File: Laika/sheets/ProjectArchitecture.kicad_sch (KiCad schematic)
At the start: 0 parts

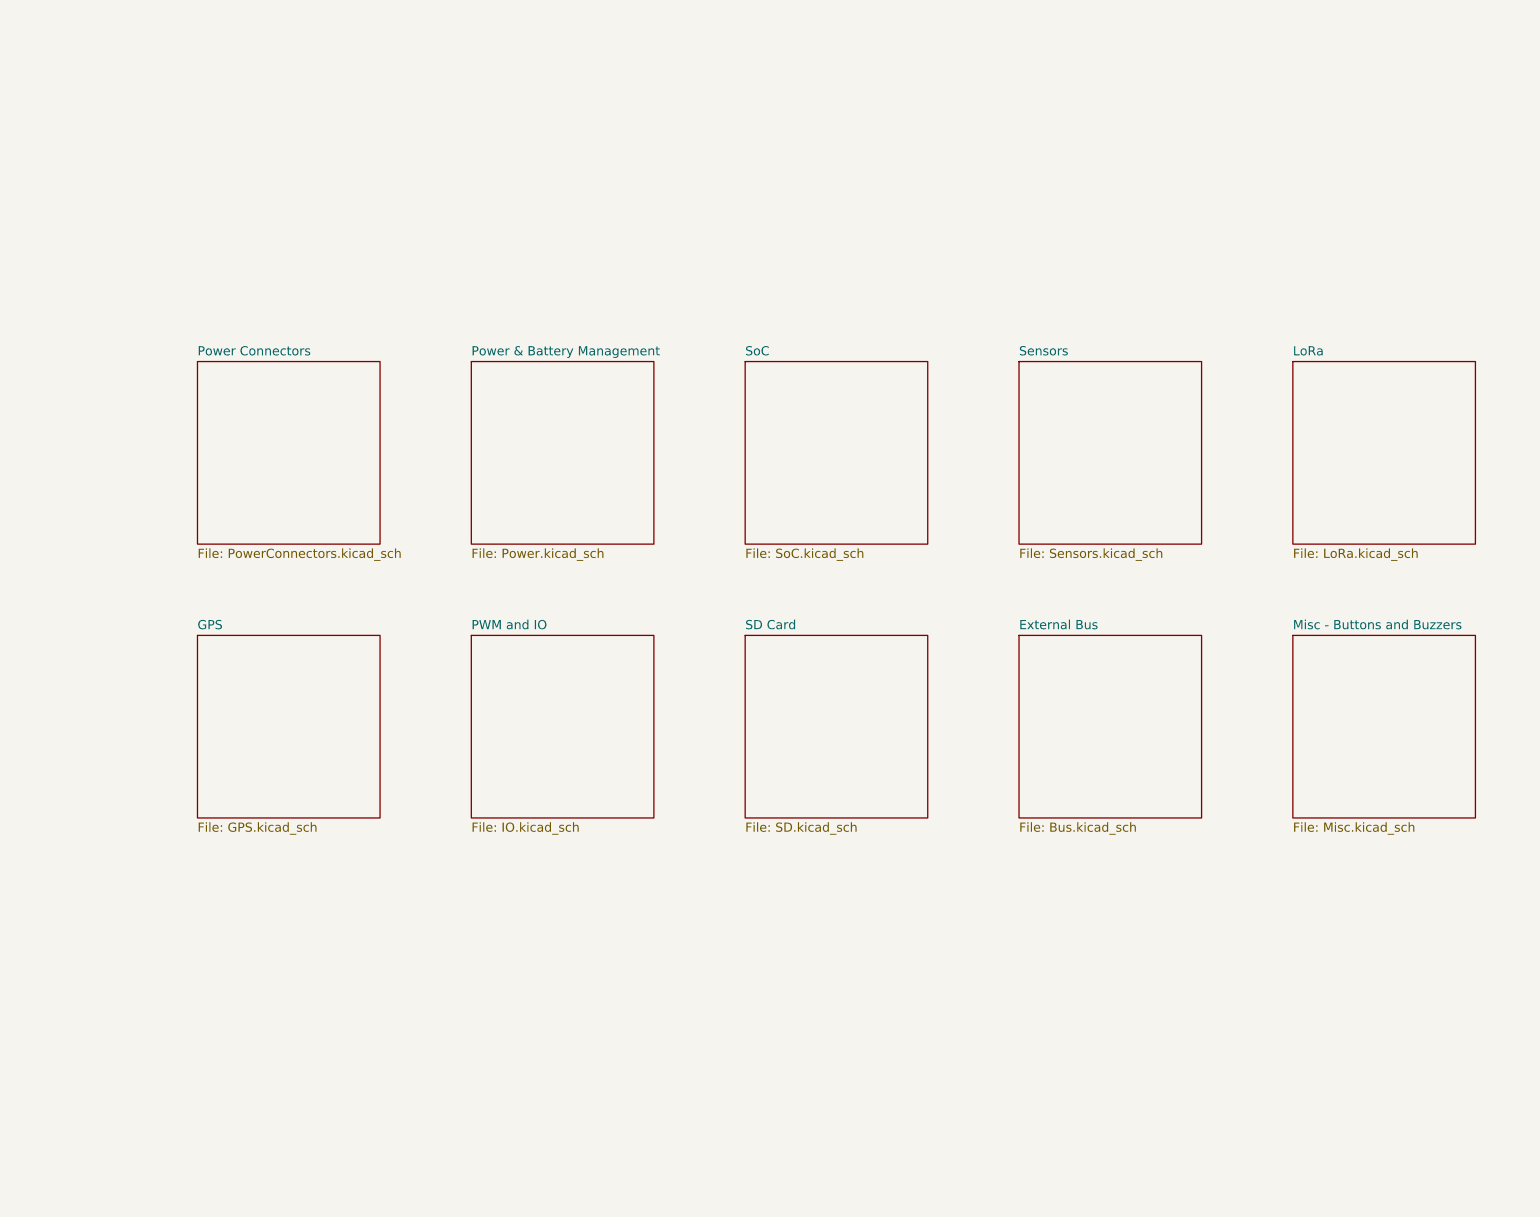
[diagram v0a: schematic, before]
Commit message: Connected USB data in schematic, adjusted Project Architecture
Adjusted the Project Architecture sheet and connected USB between the
Power Connector and SoC sheet. Cleaned up look of the Project
Architecture sheet. Added submodules for Milk V symbols and footprints.
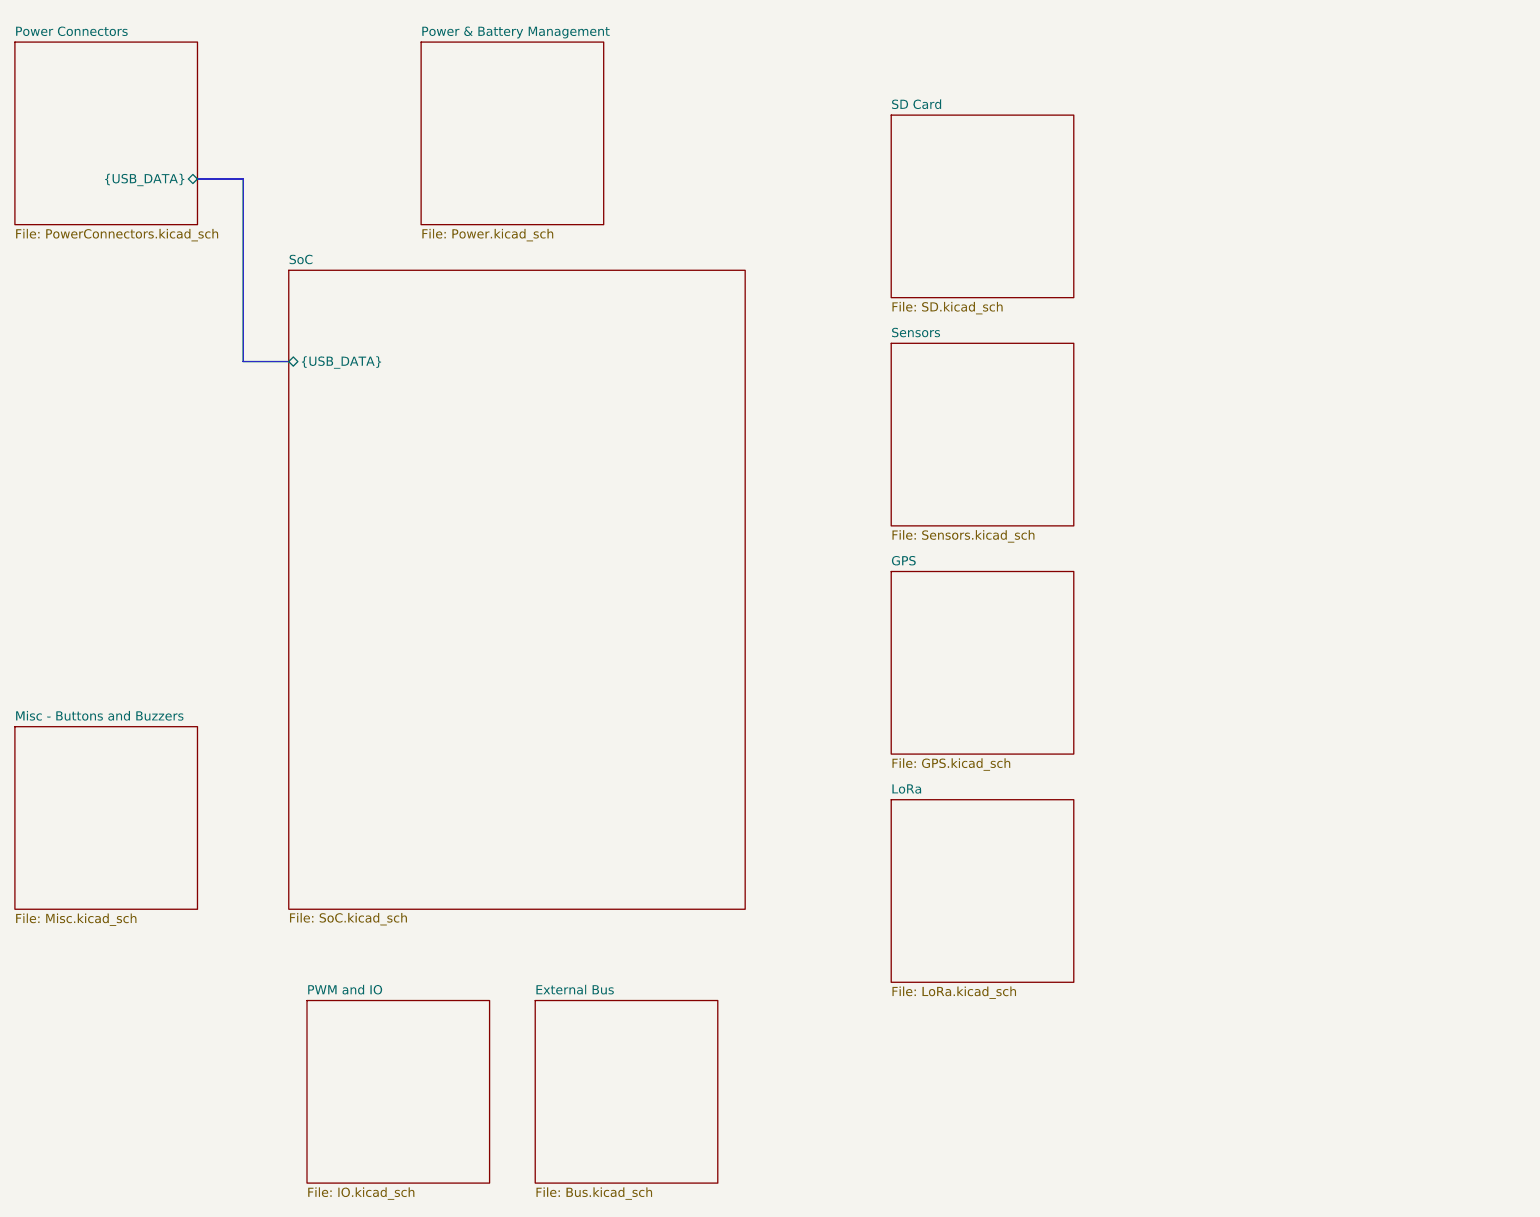
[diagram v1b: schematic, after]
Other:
- sheet Power Connectors ports: added {USB_DATA}; removed none
- sheet SoC ports: added {USB_DATA}; removed none
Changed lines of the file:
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@@
 		(comment 1 "${VARIANT}")
 	)
-	(sheet
-		(at 215.9 101.6)
+	(bus
+		(pts
+			(xy 69.85 63.5) (xy 69.85 38.1)
+		)
+		(stroke
+			(width 0)
+			(type default)
+		)
+	)
+	(bus
+		(pts
+			(xy 76.2 63.5) (xy 69.85 63.5)
+		)
+		(stroke
+			(width 0)
+			(type default)
+		)
+	)
+	(bus
+		(pts
+			(xy 69.85 38.1) (xy 63.5 38.1)
+		)
+		(stroke
+			(width 0)
+			(type default)
+		)
+	)
+	(sheet
+		(at 38.1 114.3)
 		(size 25.4 25.4)
 		(exclude_from_sim no)
@@
 		)
 		(property "Sheetname" "Misc - Buttons and Buzzers"
-			(at 215.9 100.8884 0)
+			(at 38.1 113.5884 0)
 			(effects
 				(font
@@
 		)
 		(property "Sheetfile" "Misc.kicad_sch"
-			(at 215.9 127.5846 0)
+			(at 38.1 140.2846 0)
 			(effects
 				(font
@@
 	)
 	(sheet
-		(at 177.8 101.6)
+		(at 110.49 152.4)
 		(size 25.4 25.4)
 		(exclude_from_sim no)
@@
 		)
 		(property "Sheetname" "External Bus"
-			(at 177.8 100.8884 0)
+			(at 110.49 151.6884 0)
 			(effects
 				(font
@@
 		)
 		(property "Sheetfile" "Bus.kicad_sch"
-			(at 177.8 127.5846 0)
+			(at 110.49 178.3846 0)
 			(effects
 				(font
@@
 	)
 	(sheet
-		(at 63.5 101.6)
+		(at 160.02 92.71)
 		(size 25.4 25.4)
 		(exclude_from_sim no)
@@
 		)
 		(property "Sheetname" "GPS"
-			(at 63.5 100.8884 0)
+			(at 160.02 91.9984 0)
 			(effects
 				(font
@@
 		)
 		(property "Sheetfile" "GPS.kicad_sch"
-			(at 63.5 127.5846 0)
+			(at 160.02 118.6946 0)
 			(effects
 				(font
@@
 	)
 	(sheet
-		(at 215.9 63.5)
+		(at 160.02 124.46)
 		(size 25.4 25.4)
 		(exclude_from_sim no)
@@
 		)
 		(property "Sheetname" "LoRa"
-			(at 215.9 62.7884 0)
+			(at 160.02 123.7484 0)
 			(effects
 				(font
@@
 		)
 		(property "Sheetfile" "LoRa.kicad_sch"
-			(at 215.9 89.4846 0)
+			(at 160.02 150.4446 0)
 			(effects
 				(font
@@
 	)
 	(sheet
-		(at 139.7 101.6)
+		(at 160.02 29.21)
 		(size 25.4 25.4)
 		(exclude_from_sim no)
@@
 		)
 		(property "Sheetname" "SD Card"
-			(at 139.7 100.8884 0)
+			(at 160.02 28.4984 0)
 			(effects
 				(font
@@
 		)
 		(property "Sheetfile" "SD.kicad_sch"
-			(at 139.7 127.5846 0)
+			(at 160.02 55.1946 0)
 			(effects
 				(font
@@
 	)
 	(sheet
-		(at 63.5 63.5)
+		(at 38.1 19.05)
 		(size 25.4 25.4)
 		(exclude_from_sim no)
@@
 		)
 		(property "Sheetname" "Power Connectors"
-			(at 63.5 62.7884 0)
+			(at 38.1 18.3384 0)
 			(effects
 				(font
@@
 		)
 		(property "Sheetfile" "PowerConnectors.kicad_sch"
-			(at 63.5 89.4846 0)
-			(effects
-				(font
-					(size 1.27 1.27)
-				)
-				(justify left top)
+			(at 38.1 45.0346 0)
+			(effects
+				(font
+					(size 1.27 1.27)
+				)
+				(justify left top)
+			)
+		)
+		(pin "{USB_DATA}" bidirectional
+			(at 63.5 38.1 0)
+			(effects
+				(font
+					(size 1.27 1.27)
+				)
+				(justify right)
 			)
 		)
@@
 	)
 	(sheet
-		(at 101.6 101.6)
+		(at 78.74 152.4)
 		(size 25.4 25.4)
 		(exclude_from_sim no)
@@
 		)
 		(property "Sheetname" "PWM and IO"
-			(at 101.6 100.8884 0)
+			(at 78.74 151.6884 0)
 			(effects
 				(font
@@
 		)
 		(property "Sheetfile" "IO.kicad_sch"
-			(at 101.6 127.5846 0)
+			(at 78.74 178.3846 0)
 			(effects
 				(font
@@
 	)
 	(sheet
-		(at 139.7 63.5)
-		(size 25.4 25.4)
-		(exclude_from_sim no)
-		(in_bom yes)
-		(on_board yes)
-		(dnp no)
-		(fields_autoplaced yes)
+		(at 76.2 50.8)
+		(size 63.5 88.9)
+		(exclude_from_sim no)
+		(in_bom yes)
+		(on_board yes)
+		(dnp no)
 		(stroke
 			(width 0.1524)
@@
 		)
 		(property "Sheetname" "SoC"
-			(at 139.7 62.7884 0)
+			(at 76.2 50.0884 0)
 			(effects
 				(font
@@
 		)
 		(property "Sheetfile" "SoC.kicad_sch"
-			(at 139.7 89.4846 0)
-			(effects
-				(font
-					(size 1.27 1.27)
-				)
-				(justify left top)
+			(at 76.2 140.208 0)
+			(effects
+				(font
+					(size 1.27 1.27)
+				)
+				(justify left top)
+			)
+		)
+		(pin "{USB_DATA}" bidirectional
+			(at 76.2 63.5 180)
+			(effects
+				(font
+					(size 1.27 1.27)
+				)
+				(justify left)
 			)
 		)
@@
 	)
 	(sheet
-		(at 177.8 63.5)
+		(at 160.02 60.96)
 		(size 25.4 25.4)
 		(exclude_from_sim no)
@@
 		)
 		(property "Sheetname" "Sensors"
-			(at 177.8 62.7884 0)
+			(at 160.02 60.2484 0)
 			(effects
 				(font
@@
 		)
 		(property "Sheetfile" "Sensors.kicad_sch"
-			(at 177.8 89.4846 0)
+			(at 160.02 86.9446 0)
 			(effects
 				(font
@@
 	)
 	(sheet
-		(at 101.6 63.5)
+		(at 94.615 19.05)
 		(size 25.4 25.4)
 		(exclude_from_sim no)
@@
 		)
 		(property "Sheetname" "Power & Battery Management"
-			(at 101.6 62.7884 0)
+			(at 94.615 18.3384 0)
 			(effects
 				(font
@@
 		)
 		(property "Sheetfile" "Power.kicad_sch"
-			(at 101.6 89.4846 0)
-			(effects
-				(font
+			(at 94.615 45.0346 0)
+			(effects
+				(font

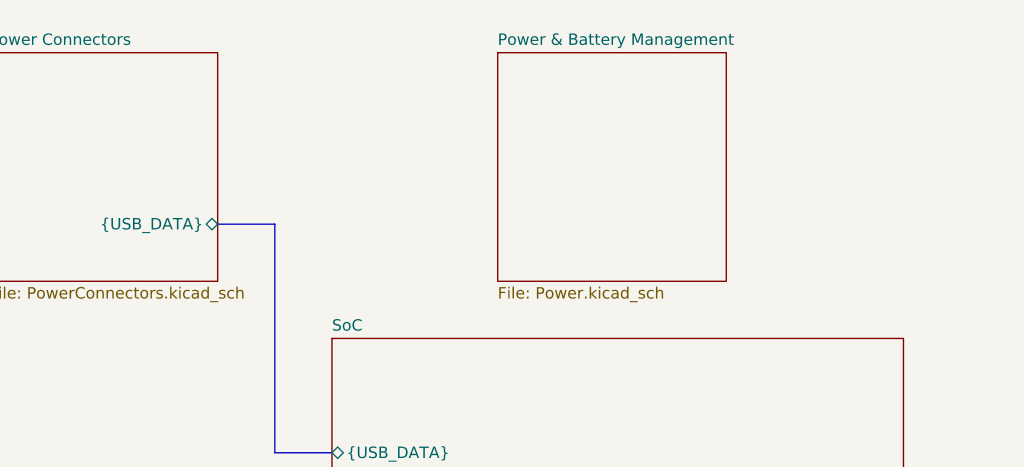
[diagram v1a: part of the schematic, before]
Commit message: Created 3.3V Buck Regulator Circuit
Created schematic for a 3.3V buck regulator. All component selection and
calaculation was performed using TI WEBENCH Power designer, of which the
artifacts are stored in 'calc'. Created Netclasses for PWR and USB.
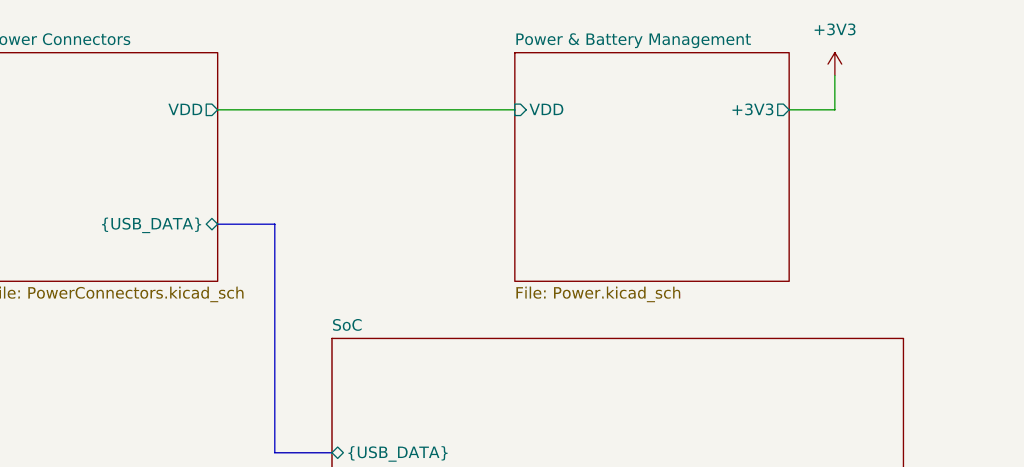
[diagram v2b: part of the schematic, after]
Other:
- sheet Power & Battery Management ports: added +3V3, VDD; removed none
- sheet Power Connectors ports: added VDD; removed none
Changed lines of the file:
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@@
 		(comment 1 "${VARIANT}")
+	)
+	(wire
+		(pts
+			(xy 63.5 25.4) (xy 96.52 25.4)
+		)
+		(stroke
+			(width 0)
+			(type default)
+		)
 	)
 	(bus
@@
 		)
 	)
+	(wire
+		(pts
+			(xy 127 25.4) (xy 132.08 25.4)
+		)
+		(stroke
+			(width 0)
+			(type default)
+		)
+	)
 	(bus
 		(pts
@@
 		)
 	)
+	(wire
+		(pts
+			(xy 132.08 21.59) (xy 132.08 25.4)
+		)
+		(stroke
+			(width 0)
+			(type default)
+		)
+	)
+	(symbol
+		(lib_id "power:+3V3")
+		(at 132.08 21.59 0)
+		(unit 1)
+		(exclude_from_sim no)
+		(in_bom yes)
+		(on_board yes)
+		(dnp no)
+		(fields_autoplaced yes)
+		(property "Reference" "#PWR08"
+			(at 132.08 25.4 0)
+			(effects
+				(font
+					(size 1.27 1.27)
+				)
+				(hide yes)
+			)
+		)
+		(property "Value" "+3V3"
+			(at 132.08 16.51 0)
+			(effects
+				(font
+					(size 1.27 1.27)
+				)
+			)
+		)
+		(property "Footprint" ""
+			(at 132.08 21.59 0)
+			(effects
+				(font
+					(size 1.27 1.27)
+				)
+				(hide yes)
+			)
+		)
+		(property "Datasheet" ""
+			(at 132.08 21.59 0)
+			(effects
+				(font
+					(size 1.27 1.27)
+				)
+				(hide yes)
+			)
+		)
+		(property "Description" "Power symbol creates a global label with name \"+3V3\""
+			(at 132.08 21.59 0)
+			(effects
+				(font
+					(size 1.27 1.27)
+				)
+				(hide yes)
+			)
+		)
+		(pin "1"
+		)
+		(instances
+			(project ""
+				(path "/57baccbf-5d29-4714-8f2e-7e9f593fcdf8/6c078d98-f795-4bff-ba6d-ace5d579e960"
+					(reference "#PWR08")
+					(unit 1)
+				)
+			)
+		)
+	)
 	(sheet
 		(at 38.1 114.3)
@@
 			)
 		)
+		(pin "VDD" output
+			(at 63.5 25.4 0)
+			(effects
+				(font
+					(size 1.27 1.27)
+				)
+				(justify right)
+			)
+		)
 		(instances
 			(project "Laika"
@@
 	)
 	(sheet
-		(at 94.615 19.05)
-		(size 25.4 25.4)
+		(at 96.52 19.05)
+		(size 30.48 25.4)
 		(exclude_from_sim no)
 		(in_bom yes)
@@
 		)
 		(property "Sheetname" "Power & Battery Management"
-			(at 94.615 18.3384 0)
+			(at 96.52 18.3384 0)
 			(effects
 				(font
@@
 		)
 		(property "Sheetfile" "Power.kicad_sch"
-			(at 94.615 45.0346 0)
-			(effects
-				(font
-					(size 1.27 1.27)
-				)
-				(justify left top)
-			)
-		)
+			(at 96.52 45.0346 0)
+			(effects
+				(font
+					(size 1.27 1.27)
+				)
+				(justify left top)
+			)
+		)
+		(pin "VDD" input
+			(at 96.52 25.4 180)
+			(effects
+				(font
+					(size 1.27 1.27)
+				)
+				(justify left)
+			)
+		)
+		(pin "+3V3" output
+			(at 127 25.4 0)
+			(effects
+				(font
+					(size 1.27 1.27)
+				)
+				(justify right)
+			)
+		)

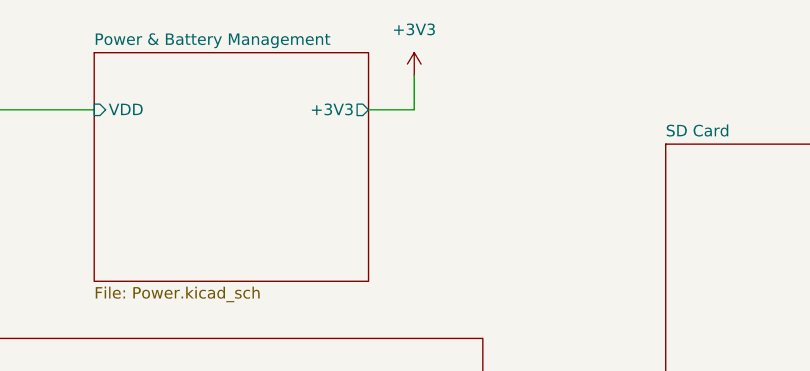
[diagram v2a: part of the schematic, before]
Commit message: Created 1.8V LDO circuit, assigned Mfr Part Numbers to Power IC's
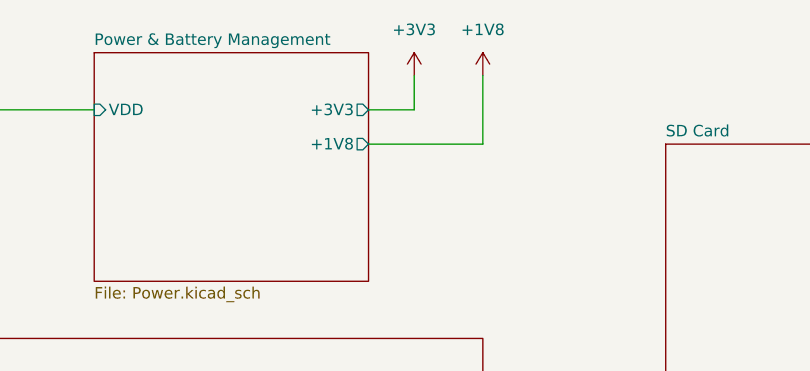
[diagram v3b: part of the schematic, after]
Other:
- sheet Power & Battery Management ports: added +1V8; removed none
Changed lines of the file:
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@@
+		)
+	)
+	(wire
+		(pts
+			(xy 127 29.21) (xy 139.7 29.21)
+		)
+		(stroke
+			(width 0)
+			(type default)
 		)
 	)
@@
 	(wire
 		(pts
-			(xy 132.08 21.59) (xy 132.08 25.4)
+			(xy 139.7 21.59) (xy 139.7 29.21)
 		)
 		(stroke
 			(width 0)
 			(type default)
+		)
+	)
+	(wire
+		(pts
+			(xy 132.08 21.59) (xy 132.08 25.4)
+		)
+		(stroke
+			(width 0)
+			(type default)
+		)
+	)
+	(symbol
+		(lib_id "power:+1V8")
+		(at 139.7 21.59 0)
+		(unit 1)
+		(exclude_from_sim no)
+		(in_bom yes)
+		(on_board yes)
+		(dnp no)
+		(fields_autoplaced yes)
+		(property "Reference" "#PWR026"
+			(at 139.7 25.4 0)
+			(effects
+				(font
+					(size 1.27 1.27)
+				)
+				(hide yes)
+			)
+		)
+		(property "Value" "+1V8"
+			(at 139.7 16.51 0)
+			(effects
+				(font
+					(size 1.27 1.27)
+				)
+			)
+		)
+		(property "Footprint" ""
+			(at 139.7 21.59 0)
+			(effects
+				(font
+					(size 1.27 1.27)
+				)
+				(hide yes)
+			)
+		)
+		(property "Datasheet" ""
+			(at 139.7 21.59 0)
+			(effects
+				(font
+					(size 1.27 1.27)
+				)
+				(hide yes)
+			)
+		)
+		(property "Description" "Power symbol creates a global label with name \"+1V8\""
+			(at 139.7 21.59 0)
+			(effects
+				(font
+					(size 1.27 1.27)
+				)
+				(hide yes)
+			)
+		)
+		(pin "1"
+		)
+		(instances
+			(project ""
+				(path "/57baccbf-5d29-4714-8f2e-7e9f593fcdf8/6c078d98-f795-4bff-ba6d-ace5d579e960"
+					(reference "#PWR026")
+					(unit 1)
+				)
+			)
 		)
 	)
@@
 			(effects
 				(font
+					(size 1.27 1.27)
+				)
+				(justify right)
+			)
+		)
+		(pin "+1V8" output
+			(at 127 29.21 0)
+			(effects
+				(font
